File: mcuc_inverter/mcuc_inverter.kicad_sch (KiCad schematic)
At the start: 0 parts

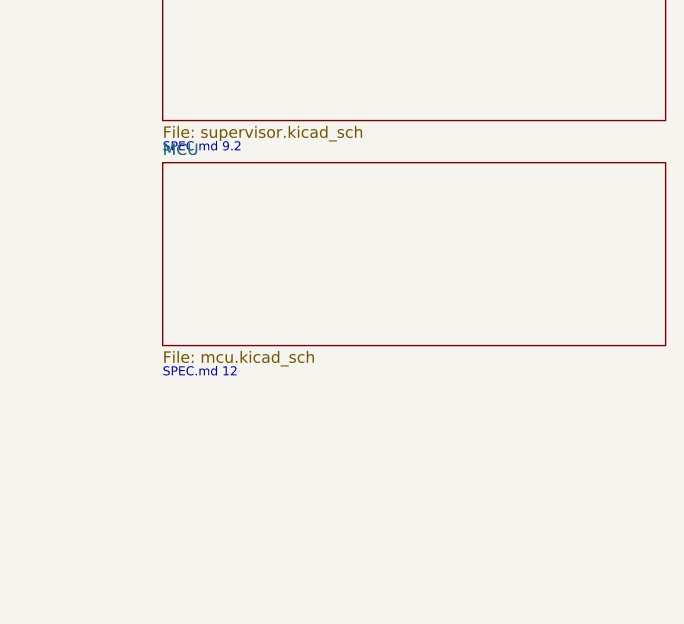
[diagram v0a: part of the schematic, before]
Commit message: Capture MCU sheet: STM32F405VGT6 core circuit, ERC clean
Populate mcuc_inverter/mcu.kicad_sch with the STM32F405VGTx from the
official KiCad 9 library: per-pin VDD decoupling (6x100n + 4.7u bulk),
VDDA/VREF+ via ferrite with 1u+100n, 2x2.2u VCAP, BOOT0 10k pulldown,
NRST 100n, 8 MHz HSE with 18 pF loads, and the SPEC 12.2 anchor pins
as hierarchical labels (TIM1 PWM HS/LS, FAULT_BKIN on PB12, CAN1,
USB, SWD) verified against the symbol pin table via netlist export.

Root sheet gains the 14 matching sheet pins on the MCU sheet symbol.
Project ERC severities: pin_not_connected and label_dangling relaxed
error->warning so future-GPIO pins stay visible without no-connect
flags (CLI ignores exclusions; label_dangling hits a known CLI false
positive on single-pin hierarchical nets, kicad#20528).

ERC: 0 errors, 93 warnings (66 unused GPIOs, 14 empty counterpart
sheets, 13 false-positive dangling labels). PDF export succeeds.

Co-Authored-By: Claude Fable 5 <noreply@anthropic.com>
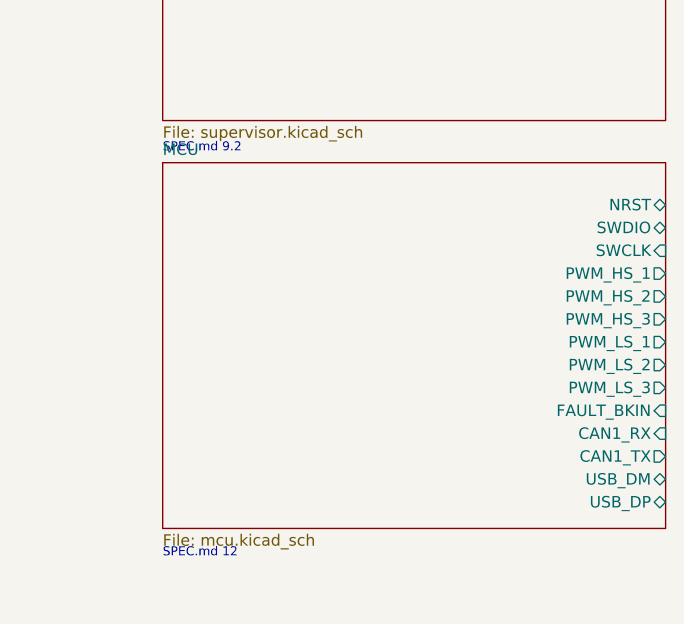
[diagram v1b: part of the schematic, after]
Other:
- sheet MCU ports: added CAN1_RX, CAN1_TX, FAULT_BKIN, NRST, PWM_HS_1, PWM_HS_2, PWM_HS_3, PWM_LS_1, PWM_LS_2, PWM_LS_3, SWCLK, SWDIO, USB_DM, USB_DP; removed none
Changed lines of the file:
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@@
 	(sheet
 		(at 160.0 135.0)
-		(size 55.88 20.32)
+		(size 55.88 40.64)
 		(fields_autoplaced yes)
 		(stroke
@@
 		)
 		(property "Sheetfile" "mcu.kicad_sch"
-			(at 160.0 155.9046 0)
+			(at 160.0 176.2246 0)
 			(effects
 				(font
@@
 				)
 				(justify left top)
+			)
+		)
+		(pin "NRST" bidirectional
+			(at 215.88 139.7 0)
+			(effects
+				(font
+					(size 1.27 1.27)
+				)
+				(justify right)
+			)
+		)
+		(pin "SWDIO" bidirectional
+			(at 215.88 142.24 0)
+			(effects
+				(font
+					(size 1.27 1.27)
+				)
+				(justify right)
+			)
+		)
+		(pin "SWCLK" input
+			(at 215.88 144.78 0)
+			(effects
+				(font
+					(size 1.27 1.27)
+				)
+				(justify right)
+			)
+		)
+		(pin "PWM_HS_1" output
+			(at 215.88 147.32 0)
+			(effects
+				(font
+					(size 1.27 1.27)
+				)
+				(justify right)
+			)
+		)
+		(pin "PWM_HS_2" output
+			(at 215.88 149.86 0)
+			(effects
+				(font
+					(size 1.27 1.27)
+				)
+				(justify right)
+			)
+		)
+		(pin "PWM_HS_3" output
+			(at 215.88 152.4 0)
+			(effects
+				(font
+					(size 1.27 1.27)
+				)
+				(justify right)
+			)
+		)
+		(pin "PWM_LS_1" output
+			(at 215.88 154.94 0)
+			(effects
+				(font
+					(size 1.27 1.27)
+				)
+				(justify right)
+			)
+		)
+		(pin "PWM_LS_2" output
+			(at 215.88 157.48 0)
+			(effects
+				(font
+					(size 1.27 1.27)
+				)
+				(justify right)
+			)
+		)
+		(pin "PWM_LS_3" output
+			(at 215.88 160.02 0)
+			(effects
+				(font
+					(size 1.27 1.27)
+				)
+				(justify right)
+			)
+		)
+		(pin "FAULT_BKIN" input
+			(at 215.88 162.56 0)
+			(effects
+				(font
+					(size 1.27 1.27)
+				)
+				(justify right)
+			)
+		)
+		(pin "CAN1_RX" input
+			(at 215.88 165.1 0)
+			(effects
+				(font
+					(size 1.27 1.27)
+				)
+				(justify right)
+			)
+		)
+		(pin "CAN1_TX" output
+			(at 215.88 167.64 0)
+			(effects
+				(font
+					(size 1.27 1.27)
+				)
+				(justify right)
+			)
+		)
+		(pin "USB_DM" bidirectional
+			(at 215.88 170.18 0)
+			(effects
+				(font
+					(size 1.27 1.27)
+				)
+				(justify right)
+			)
+		)
+		(pin "USB_DP" bidirectional
+			(at 215.88 172.72 0)
+			(effects
+				(font
+					(size 1.27 1.27)
+				)
+				(justify right)
 			)
 		)
@@
 	(text "SPEC.md 12"
 		(exclude_from_sim no)
-		(at 160.0 159.0 0)
+		(at 160.0 179.0 0)
 		(effects
 			(font

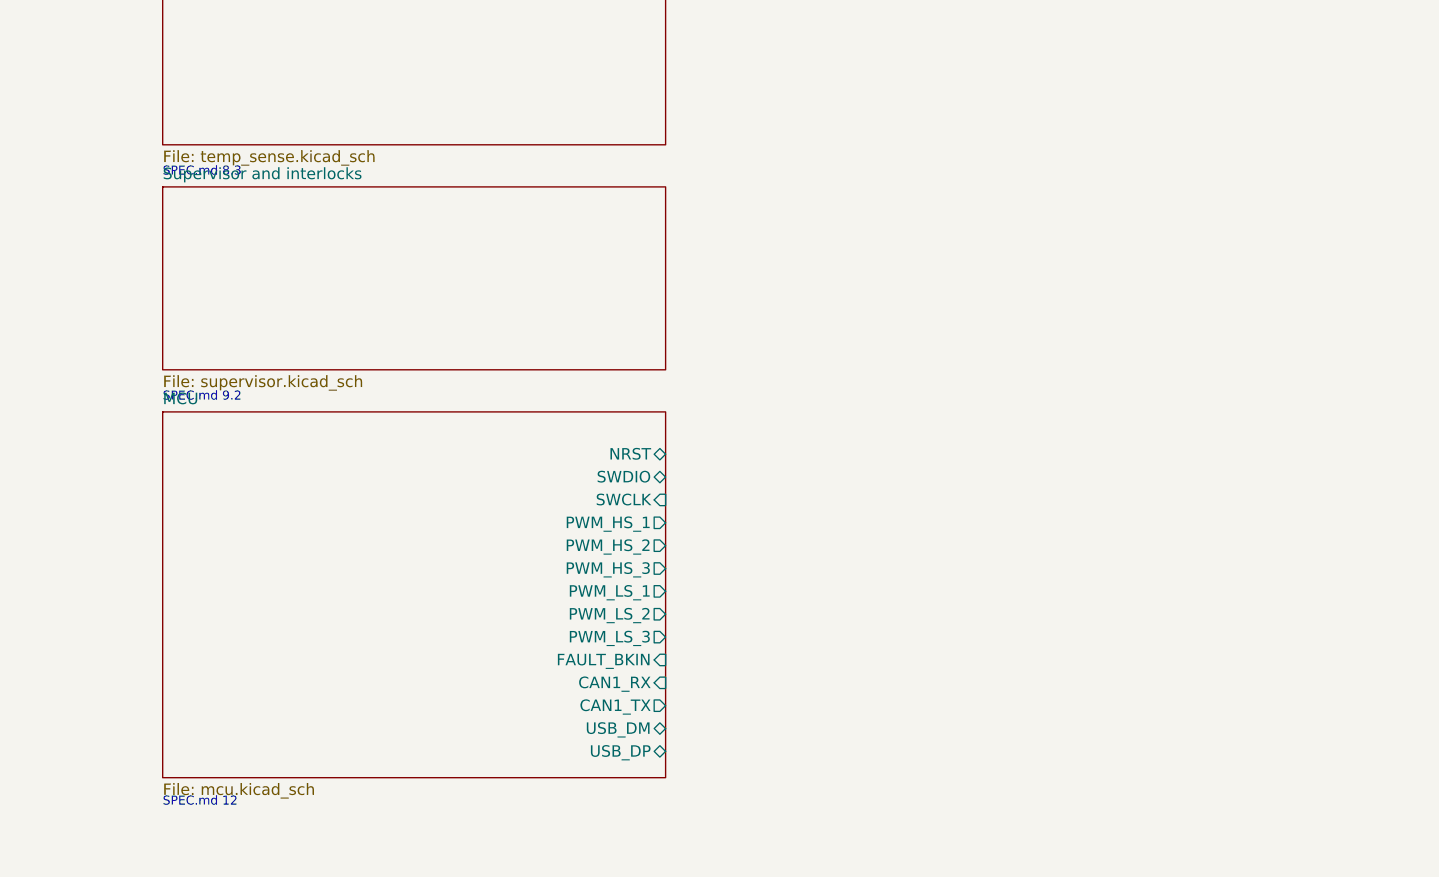
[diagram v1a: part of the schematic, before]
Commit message: Port PALTA supervisor interlocks to KiCad 9 supervisor sheet
Faithful recapture of pcb_design/supervisor.sch (verified against the
legacy VESC-controller.net netlist): per-phase NAND overlap detection
gating complementary PWM pairs through AND gates (both outputs forced
low on overlap), 4.7k boot pulldowns on all six PWM inputs, AUP1G74
overcurrent latch (OC_TRIP edge -> latched, FAULT_RESET clear, LED),
driver-fault conditioning (RC + BAT54S clamp) driving FAULT_BKIN, and
the active-low driver-reset chain (MCU request AND driver-fault AND
OC latch).

Interface: PWM_HS/LS_1..3 in, *_GATED out, OC_TRIP (single open-drain
input; comparator lives with current sensing per SPEC), DRV_FAULT_IN,
OC_LATCHED, FAULT_RESET, DRV_RST_IN/OUT. Root sheet wires the six PWM
nets and FAULT_BKIN between MCU and supervisor; FAULT_BKIN verified by
netlist to land on U1 pin 51 = PB12 (TIM1_BKIN).

ERC 0 errors. 24/24 gate-by-gate netlist checks against the legacy
reconstruction pass. Deviations recorded on-sheet: all-3.3V logic
(original BOM fitted ACT08 at 5 V), added pullups on FAULT_RESET /
DRV_RST_IN boot state.

Finding: the original circuit performs overlap elimination only - it
contains NO hardware dead-time insertion despite D008/SPEC 9.2 claiming
it. Recorded separately as a spec discrepancy.

Co-Authored-By: Claude Fable 5 <noreply@anthropic.com>
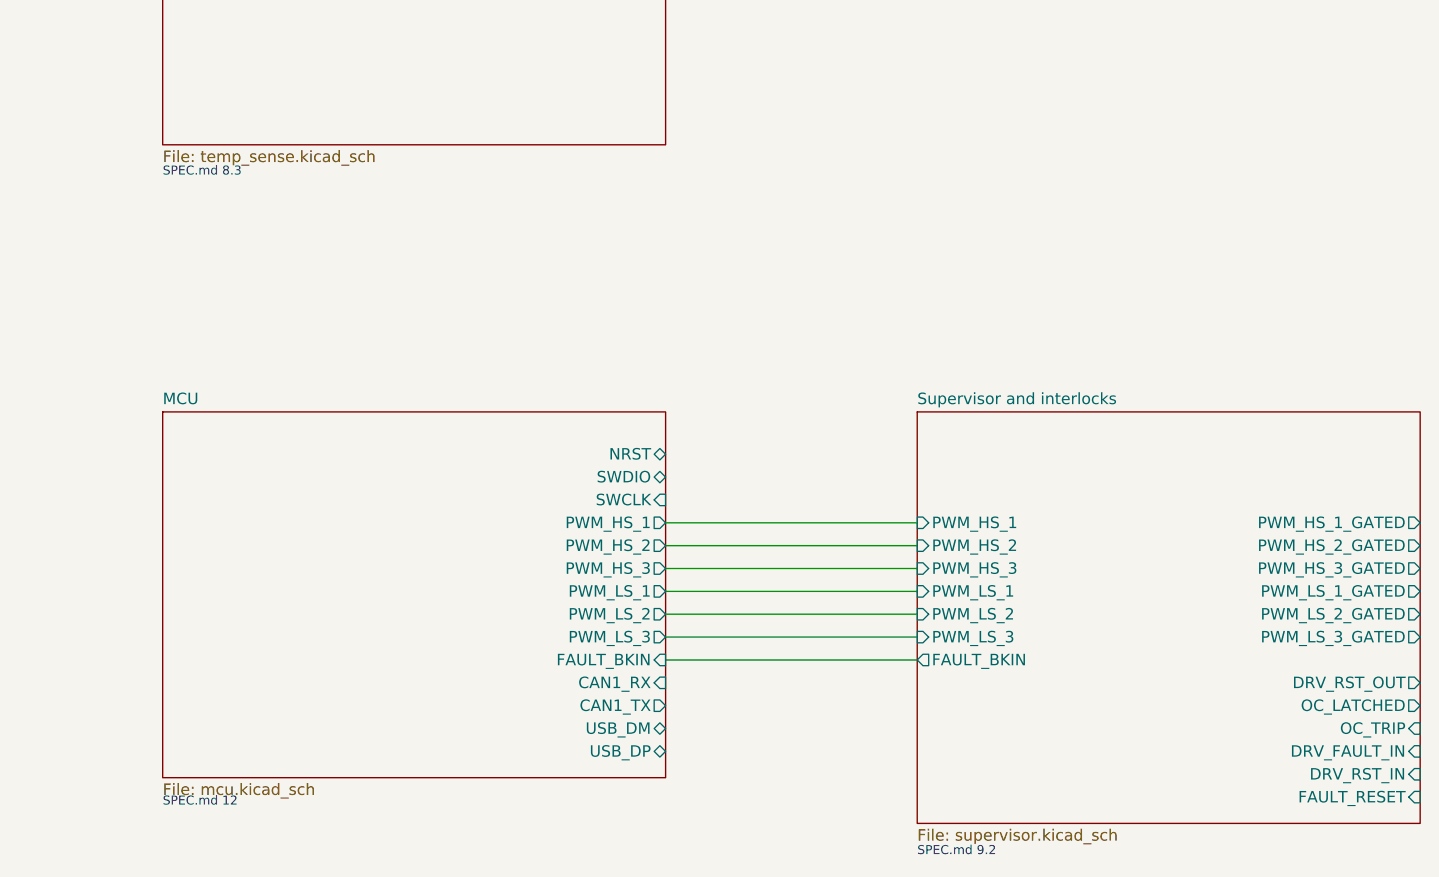
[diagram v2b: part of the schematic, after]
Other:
- sheet Supervisor and interlocks ports: added DRV_FAULT_IN, DRV_RST_IN, DRV_RST_OUT, FAULT_BKIN, FAULT_RESET, OC_LATCHED, OC_TRIP, PWM_HS_1, PWM_HS_1_GATED, PWM_HS_2, PWM_HS_2_GATED, PWM_HS_3, PWM_HS_3_GATED, PWM_LS_1, PWM_LS_1_GATED, PWM_LS_2, PWM_LS_2_GATED, PWM_LS_3, PWM_LS_3_GATED; removed none

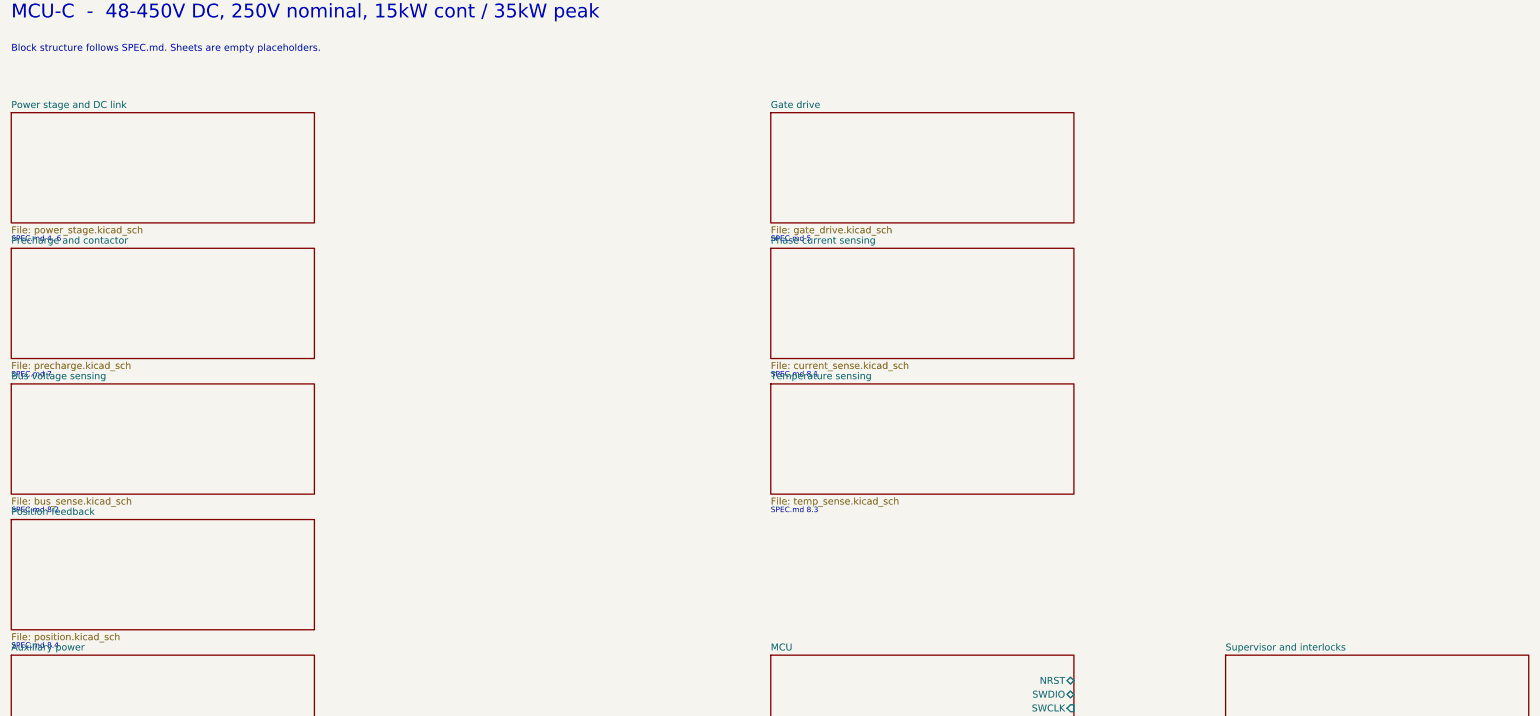
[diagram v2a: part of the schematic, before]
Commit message: Capture power_stage sheet: FS02MR12A8MA2B module + DC-link bank
Custom symbol (project lib mcuc_inverter.kicad_sym) built from the
module datasheet pin map, Fig. 1/3/4: 39 pins - G1-G6, dual Kelvin
sources S1.1..S6.2, drain-sense D1-D6, TS1-TS3 diode pairs, and 9
power terminals (P1-3/N1-3/U/V/W, per-phase DC feeds tied on-sheet,
laminated busbar note). Switch mapping odd=HS/even=LS, 1/2=U 3/4=V
5/6=W per Fig. 1.

DC-link: C201-C205, 5x 100uF 900V film [TBV], with the SPEC 6.1 bank
duty note (>=400uF, >=80 A rms @ 70C, 114 A/120 s TBV) and the
AN-G2-ASSEMBLY PressFIT pattern note.

ERC 0 errors; netlist assertion 49 pins / 29 nets, 0 mismatches.

Co-Authored-By: Claude Fable 5 <noreply@anthropic.com>
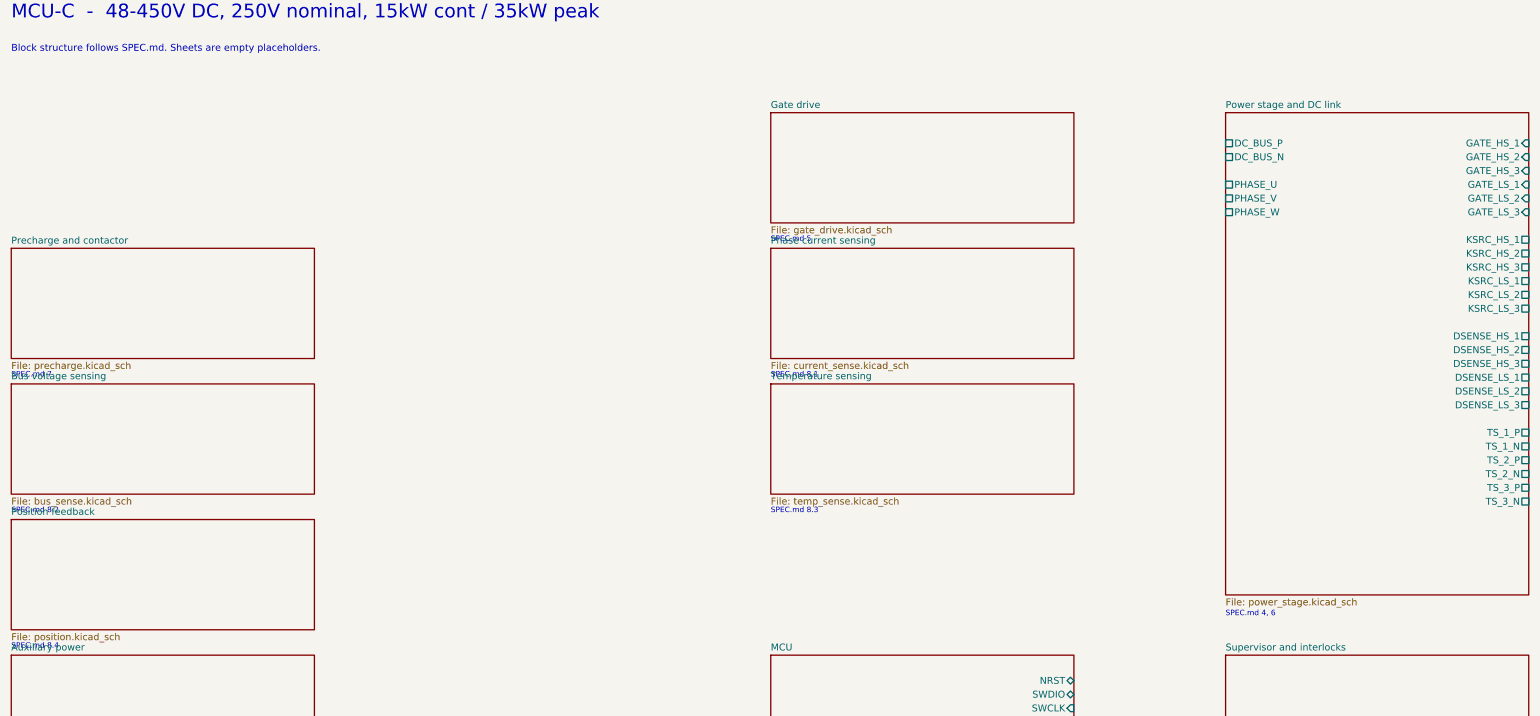
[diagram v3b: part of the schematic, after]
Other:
- sheet Power stage and DC link ports: added DC_BUS_N, DC_BUS_P, DSENSE_HS_1, DSENSE_HS_2, DSENSE_HS_3, DSENSE_LS_1, DSENSE_LS_2, DSENSE_LS_3, GATE_HS_1, GATE_HS_2, GATE_HS_3, GATE_LS_1, GATE_LS_2, GATE_LS_3, KSRC_HS_1, KSRC_HS_2, KSRC_HS_3, KSRC_LS_1, KSRC_LS_2, KSRC_LS_3, PHASE_U, PHASE_V, PHASE_W, TS_1_N, TS_1_P, TS_2_N, TS_2_P, TS_3_N, TS_3_P; removed none
